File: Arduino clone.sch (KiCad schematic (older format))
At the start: 0 parts

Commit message: Created new child sheet, added project symbols.
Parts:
- added BT?: Battery, symbol Device:Battery
- added C? (x2): C, symbol Device:C
- added C?: CP, symbol Device:CP
- added D?: LED, symbol Device:LED
- added R? (x2): R_US, symbol Device:R_US
- added U?: 24LC1025, symbol Memory_EEPROM:24LC1025
- added U?: ATmega328P-AU, Package_QFP:TQFP-32_7x7mm_P0.8mm, symbol MCU_Microchip_ATmega:ATmega328P-AU
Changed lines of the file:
@@
 $Descr A4 11693 8268
 encoding utf-8
-Sheet 1 1
+Sheet 1 2
 Title "Arduino Clone"
 Date "2021-02-01"
@@
 Comment4 ""
 $EndDescr
+$Comp
+L Device:Battery BT?
+U 1 1 601B418E
+P 2475 3125
+F 0 "BT?" H 2583 3171 50  0000 L CNN
+F 1 "Battery" H 2583 3080 50  0000 L CNN
+F 2 "" V 2475 3185 50  0001 C CNN
+F 3 "~" V 2475 3185 50  0001 C CNN
+	1    2475 3125
+	1    0    0    -1
+$EndComp
+$Comp
+L Device:C C?
+U 1 1 601B4C5C
+P 3600 3075
+F 0 "C?" H 3715 3121 50  0000 L CNN
+F 1 "C" H 3715 3030 50  0000 L CNN
+F 2 "" H 3638 2925 50  0001 C CNN
+F 3 "~" H 3600 3075 50  0001 C CNN
+	1    3600 3075
+	1    0    0    -1
+$EndComp
+$Comp
+L Device:C C?
+U 1 1 601B50D6
+P 3625 3475
+F 0 "C?" H 3740 3521 50  0000 L CNN
+F 1 "C" H 3740 3430 50  0000 L CNN
+F 2 "" H 3663 3325 50  0001 C CNN
+F 3 "~" H 3625 3475 50  0001 C CNN
+	1    3625 3475
+	1    0    0    -1
+$EndComp
+$Comp
+L Device:CP C?
+U 1 1 601B5633
+P 4425 3125
+F 0 "C?" H 4543 3171 50  0000 L CNN
+F 1 "CP" H 4543 3080 50  0000 L CNN
+F 2 "" H 4463 2975 50  0001 C CNN
+F 3 "~" H 4425 3125 50  0001 C CNN
+	1    4425 3125
+	1    0    0    -1
+$EndComp
+$Comp
+L Device:LED D?
+U 1 1 601B5CCB
+P 2475 3850
+F 0 "D?" H 2468 4067 50  0000 C CNN
+F 1 "LED" H 2468 3976 50  0000 C CNN
+F 2 "" H 2475 3850 50  0001 C CNN
+F 3 "~" H 2475 3850 50  0001 C CNN
+	1    2475 3850
+	1    0    0    -1
+$EndComp
+$Comp
+L Device:R_US R?
+U 1 1 601B6694
+P 3125 3950
+F 0 "R?" H 3193 3996 50  0000 L CNN
+F 1 "R_US" H 3193 3905 50  0000 L CNN
+F 2 "" V 3165 3940 50  0001 C CNN
+F 3 "~" H 3125 3950 50  0001 C CNN
+	1    3125 3950
+	1    0    0    -1
+$EndComp
+$Comp
+L Device:R_US R?
+U 1 1 601B6C79
+P 3500 3925
+F 0 "R?" H 3568 3971 50  0000 L CNN
+F 1 "R_US" H 3568 3880 50  0000 L CNN
+F 2 "" V 3540 3915 50  0001 C CNN
+F 3 "~" H 3500 3925 50  0001 C CNN
+	1    3500 3925
+	1    0    0    -1
+$EndComp
+$Comp
+L Memory_EEPROM:24LC1025 U?
+U 1 1 601B7371
+P 4750 3950
+F 0 "U?" H 4750 4431 50  0000 C CNN
+F 1 "24LC1025" H 4750 4340 50  0000 C CNN
+F 2 "" H 4750 3950 50  0001 C CNN
+F 3 "http://ww1.microchip.com/downloads/en/DeviceDoc/21941B.pdf" H 4750 3950 50  0001 C CNN
+	1    4750 3950
+	1    0    0    -1
+$EndComp
+$Comp
+L MCU_Microchip_ATmega:ATmega328P-AU U?
+U 1 1 601B7F08
+P 6225 3125
+F 0 "U?" H 6225 1536 50  0000 C CNN
+F 1 "ATmega328P-AU" H 6225 1445 50  0000 C CNN
+F 2 "Package_QFP:TQFP-32_7x7mm_P0.8mm" H 6225 3125 50  0001 C CIN
+F 3 "http://ww1.microchip.com/downloads/en/DeviceDoc/ATmega328_P%20AVR%20MCU%20with%20picoPower%20Technology%20Data%20Sheet%2040001984A.pdf" H 6225 3125 50  0001 C CNN
+	1    6225 3125
+	1    0    0    -1
+$EndComp
+$Sheet
+S 7500 4250 3500 2000
+U 601B8BF2
+F0 "Connectors" 50
+F1 "Connectors.sch" 50
+$EndSheet
 $EndSCHEMATC

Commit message: Added symbol for ATMEGA32p-AU.
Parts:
- removed U?: ATmega328P-AU, Package_QFP:TQFP-32_7x7mm_P0.8mm, symbol MCU_Microchip_ATmega:ATmega328P-AU
- added U?: ATMEGA328P-AU, digikey-footprints:TQFP-32_7x7mm, symbol dk_Embedded-Microcontrollers:ATMEGA328P-AU
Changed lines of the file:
@@
-	1    0    0    -1
-$EndComp
-$Comp
-L MCU_Microchip_ATmega:ATmega328P-AU U?
-U 1 1 601B7F08
-P 6225 3125
-F 0 "U?" H 6225 1536 50  0000 C CNN
-F 1 "ATmega328P-AU" H 6225 1445 50  0000 C CNN
-F 2 "Package_QFP:TQFP-32_7x7mm_P0.8mm" H 6225 3125 50  0001 C CIN
-F 3 "http://ww1.microchip.com/downloads/en/DeviceDoc/ATmega328_P%20AVR%20MCU%20with%20picoPower%20Technology%20Data%20Sheet%2040001984A.pdf" H 6225 3125 50  0001 C CNN
-	1    6225 3125
 	1    0    0    -1
 $EndComp
@@
 F1 "Connectors.sch" 50
 $EndSheet
+$Comp
+L dk_Embedded-Microcontrollers:ATMEGA328P-AU U?
+U 1 1 601BDCDB
+P 6175 2925
+F 0 "U?" H 6503 3028 60  0000 L CNN
+F 1 "ATMEGA328P-AU" H 6503 2922 60  0000 L CNN
+F 2 "digikey-footprints:TQFP-32_7x7mm" H 6375 3125 60  0001 L CNN
+F 3 "http://www.microchip.com/mymicrochip/filehandler.aspx?ddocname=en608326" H 6375 3225 60  0001 L CNN
+F 4 "ATMEGA328P-AU-ND" H 6375 3325 60  0001 L CNN "Digi-Key_PN"
+F 5 "ATMEGA328P-AU" H 6375 3425 60  0001 L CNN "MPN"
+F 6 "Integrated Circuits (ICs)" H 6375 3525 60  0001 L CNN "Category"
+F 7 "Embedded - Microcontrollers" H 6375 3625 60  0001 L CNN "Family"
+F 8 "http://www.microchip.com/mymicrochip/filehandler.aspx?ddocname=en608326" H 6375 3725 60  0001 L CNN "DK_Datasheet_Link"
+F 9 "/product-detail/en/microchip-technology/ATMEGA328P-AU/ATMEGA328P-AU-ND/1832260" H 6375 3825 60  0001 L CNN "DK_Detail_Page"
+F 10 "IC MCU 8BIT 32KB FLASH 32TQFP" H 6375 3925 60  0001 L CNN "Description"
+F 11 "Microchip Technology" H 6375 4025 60  0001 L CNN "Manufacturer"
+F 12 "Active" H 6375 4125 60  0001 L CNN "Status"
+	1    6175 2925
+	1    0    0    -1
+$EndComp
 $EndSCHEMATC

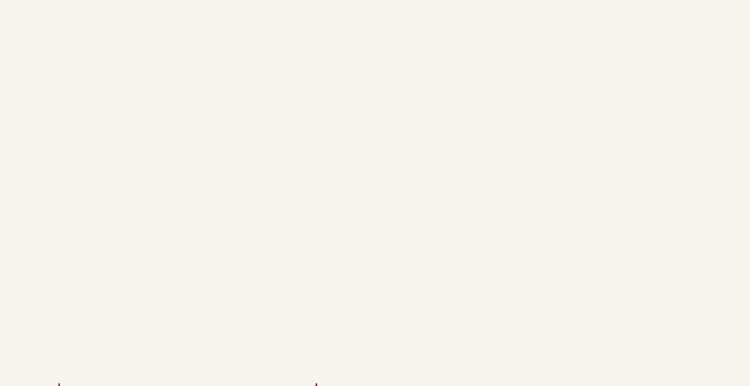
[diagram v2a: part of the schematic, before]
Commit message: Created clock IC and added the 2 crystals.
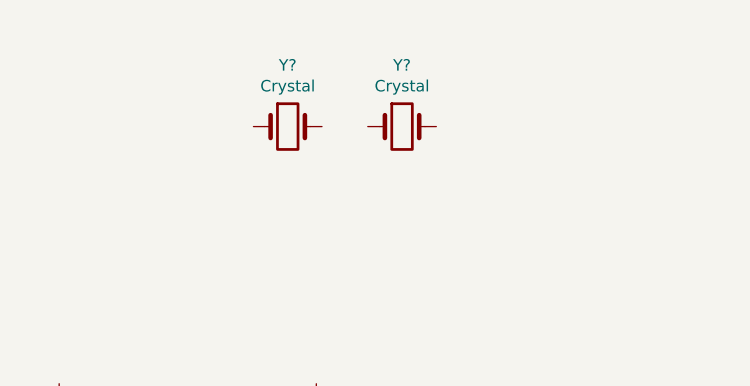
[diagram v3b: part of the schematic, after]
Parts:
- added Y? (x2): Crystal, symbol Device:Crystal
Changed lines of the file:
@@
+	1    0    0    -1
+$EndComp
+$Comp
+L Device:Crystal Y?
+U 1 1 601C298C
+P 3475 1800
+F 0 "Y?" H 3475 2068 50  0000 C CNN
+F 1 "Crystal" H 3475 1977 50  0000 C CNN
+F 2 "" H 3475 1800 50  0001 C CNN
+F 3 "~" H 3475 1800 50  0001 C CNN
+	1    3475 1800
+	1    0    0    -1
+$EndComp
+$Comp
+L Device:Crystal Y?
+U 1 1 601C36A9
+P 3975 1800
+F 0 "Y?" H 3975 2068 50  0000 C CNN
+F 1 "Crystal" H 3975 1977 50  0000 C CNN
+F 2 "" H 3975 1800 50  0001 C CNN
+F 3 "~" H 3975 1800 50  0001 C CNN
+	1    3975 1800
 	1    0    0    -1
 $EndComp

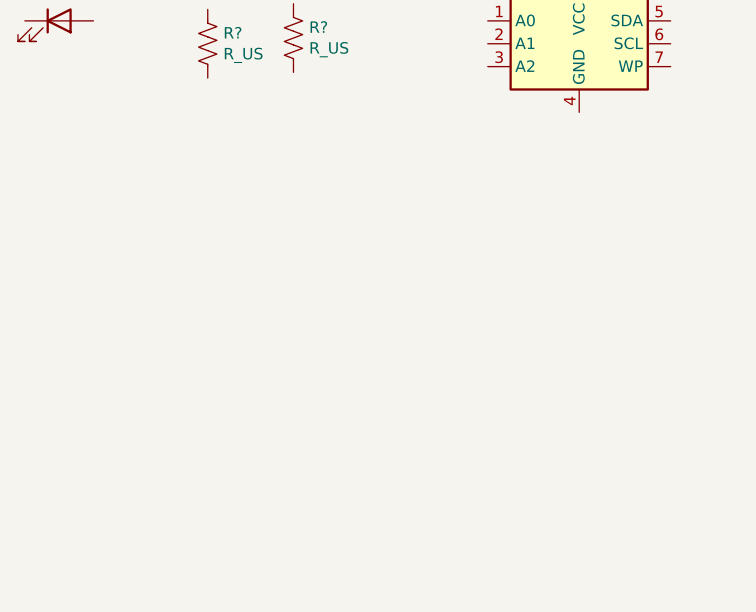
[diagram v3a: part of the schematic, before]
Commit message: Added clock IC to schematic
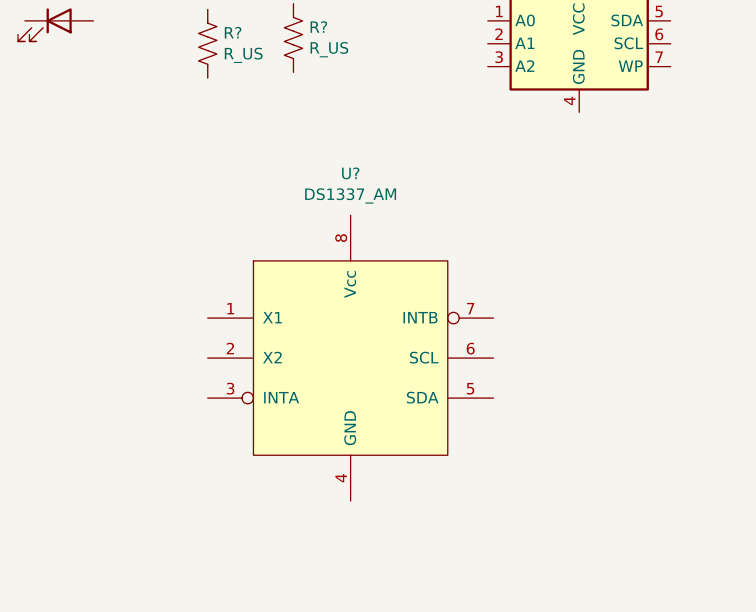
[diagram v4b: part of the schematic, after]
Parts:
- added U?: DS1337_AM, symbol Abtahi's_Library:DS1337_AM
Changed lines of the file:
@@
+	1    0    0    -1
+$EndComp
+$Comp
+L Abtahi's_Library:DS1337_AM U?
+U 1 1 601C4304
+P 3750 5325
+F 0 "U?" H 3750 6131 50  0000 C CNN
+F 1 "DS1337_AM" H 3750 6040 50  0000 C CNN
+F 2 "" H 3750 5325 50  0001 C CNN
+F 3 "" H 3750 5325 50  0001 C CNN
+	1    3750 5325
 	1    0    0    -1
 $EndComp
